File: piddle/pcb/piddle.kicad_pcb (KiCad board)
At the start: 2 copper layers, 138.6 x 138 mm, 88 parts, among them J1 Conn_01x03_Socket, J10 Conn_01x03_Socket, J11 Conn_01x03_Socket, J12 Conn_01x03_Socket, J13 Conn_01x03_Socket, J14 Conn_01x03_Socket, J15 Conn_01x03_Socket, J16 infrared receiver, J17 5v, J18 3v3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

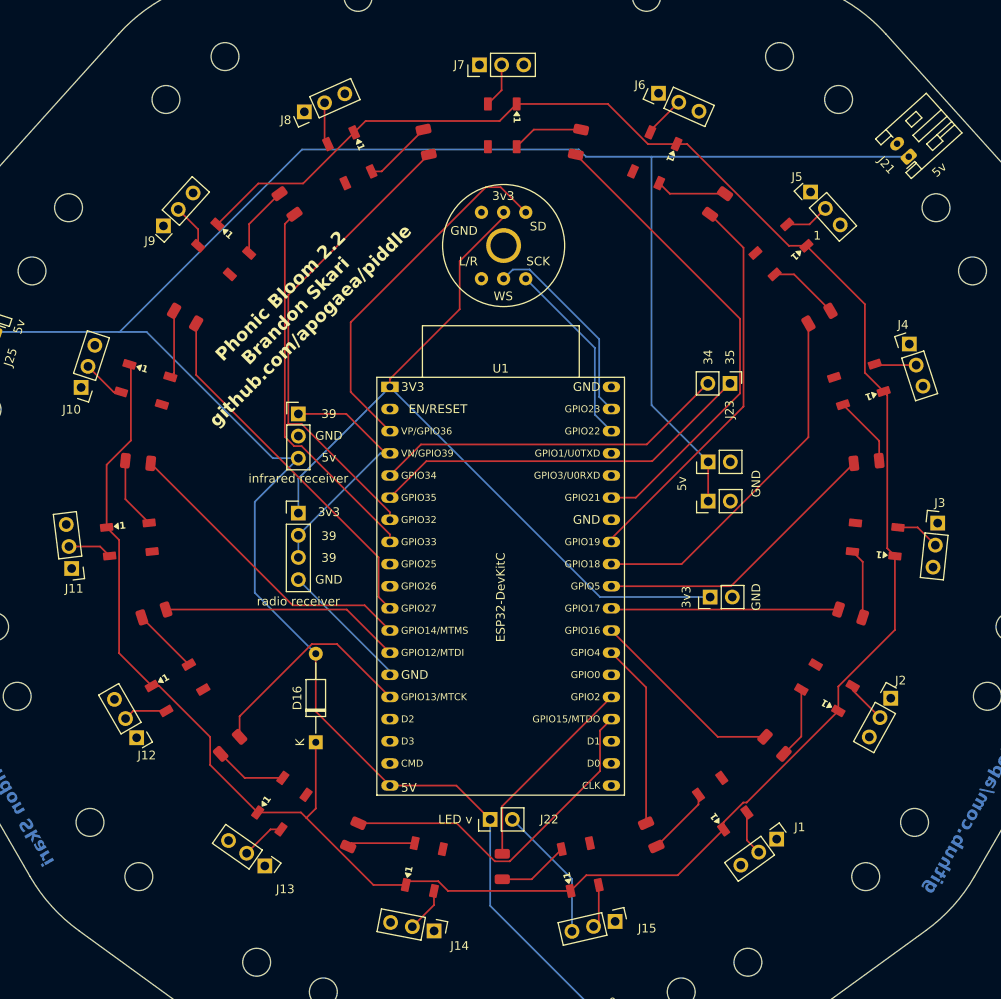
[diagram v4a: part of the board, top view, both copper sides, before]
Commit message: Clean up footprints from DRC
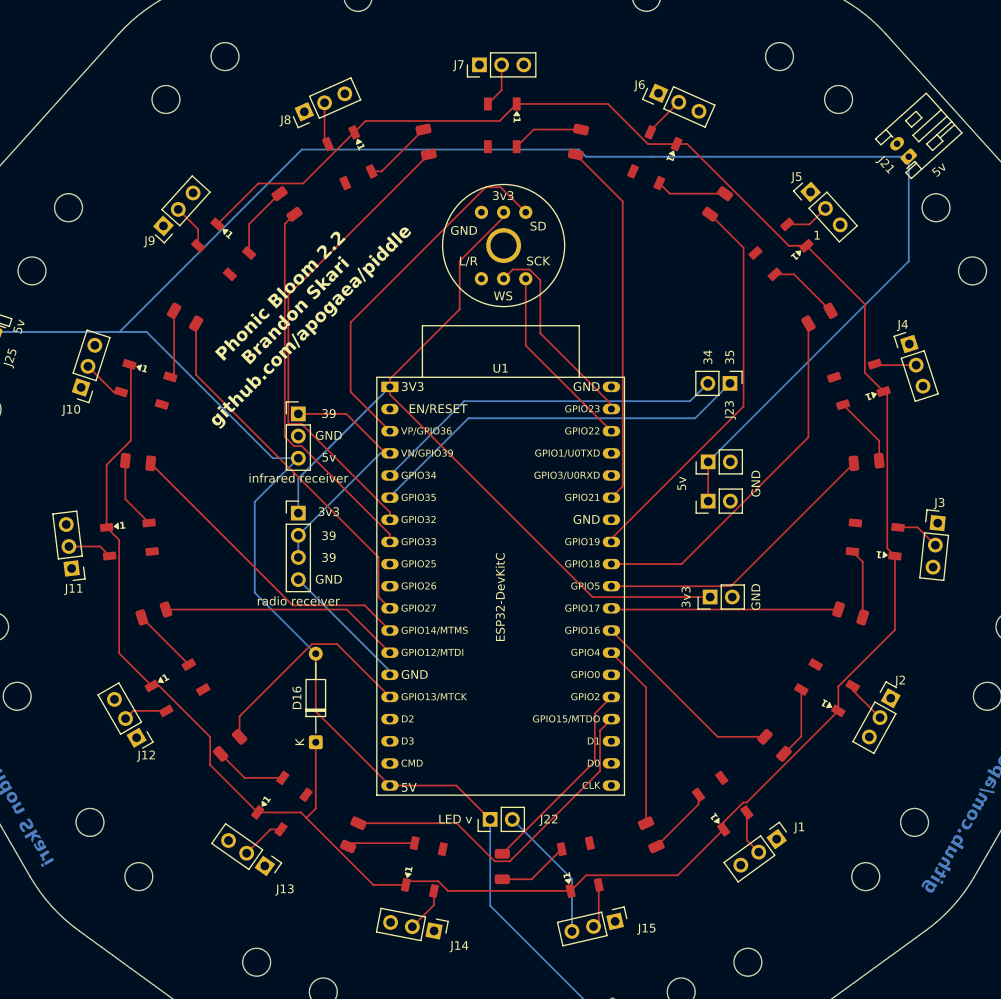
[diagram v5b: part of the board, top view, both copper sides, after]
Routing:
- net /GPIO21: track 54.9 -> 42.1 mm
- net +5V: track 270.9 -> 277.8 mm
- net +3.3V: track 91.1 -> 91.6 mm
